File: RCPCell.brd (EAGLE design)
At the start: 99.8 x 80 mm, 22 parts, among them IC1 SIM900, Q1 BSS84, Q2 BSS84, U1 PESDXS4UD

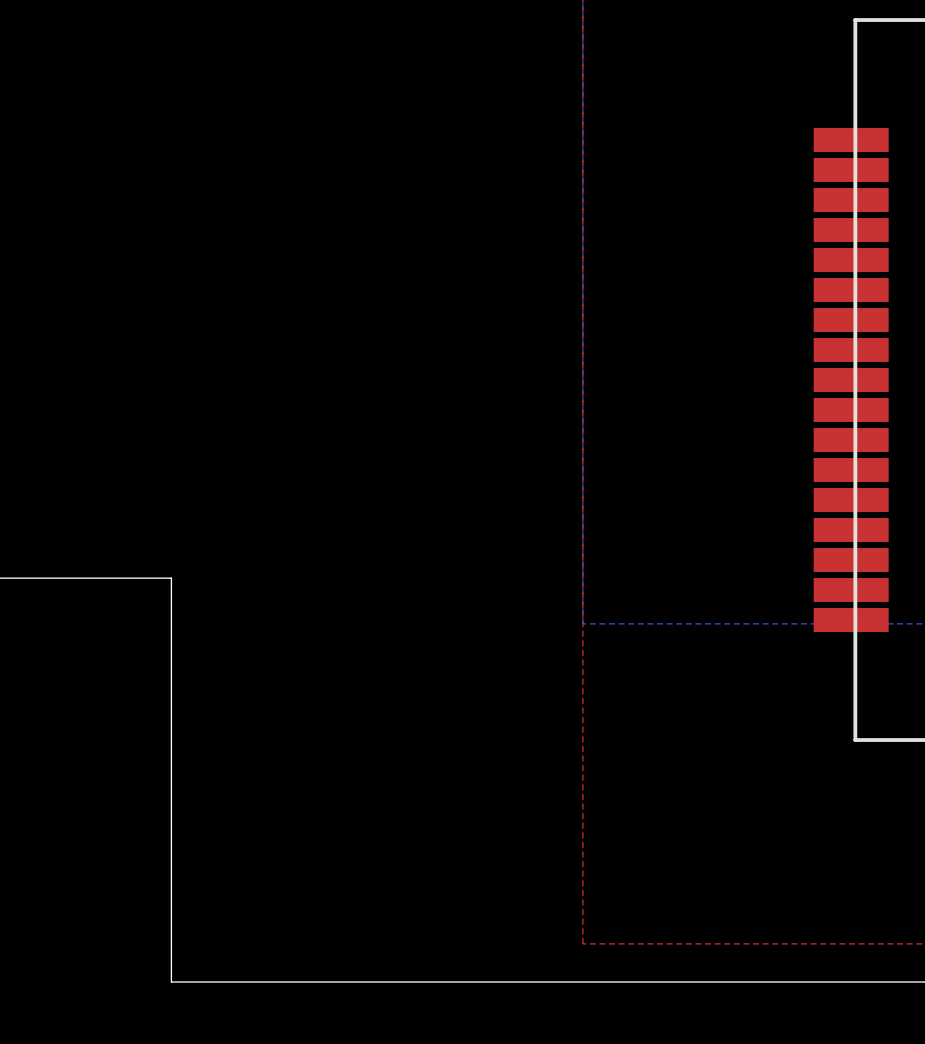
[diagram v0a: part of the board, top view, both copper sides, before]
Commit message: placeholder simcard
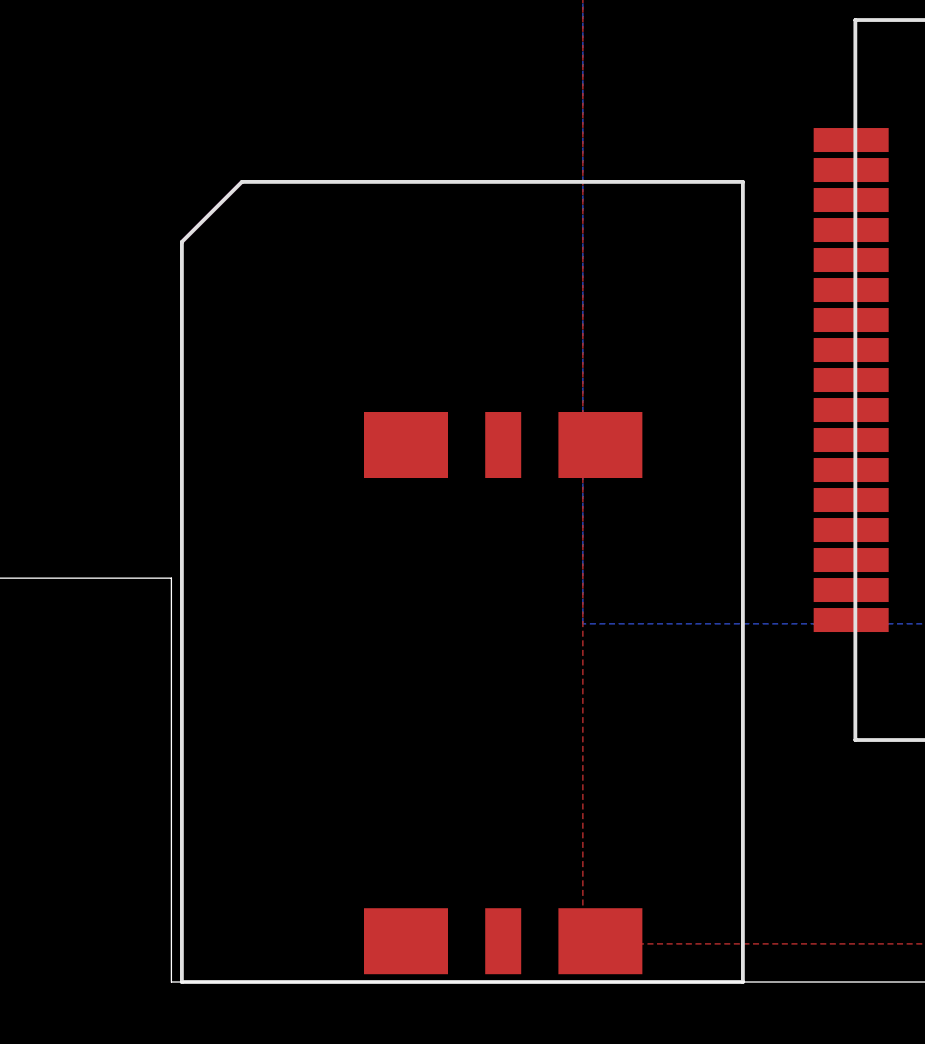
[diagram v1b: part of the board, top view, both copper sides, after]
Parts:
- added U$1: MOLEX_0470230001, simcard:MOLEX_0470230001
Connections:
- net GND: now also U$1.6
- net SIM_CLK_CARD: now also U$1.3
- net SIM_DATA_CARD: now also U$1.4
- net SIM_RST_CARD: now also U$1.2
- net SIM_VDD: now also U$1.1
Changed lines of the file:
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@@
 </element>
 <element name="J$1" library="SparkFun" package="SMA-EDGE" value="SMA_EDGE" x="74.168" y="3.8481"/>
+<element name="U$1" library="simcard" package="MOLEX_0470230001" value="MOLEX_0470230001" x="60.96" y="0" rot="R90"/>
 </elements>
 <signals>
@@
 <contactref element="J$1" pad="GND@1"/>
 <contactref element="J$1" pad="GND@0"/>
+<contactref element="U$1" pad="6"/>
 <wire x1="107.95" y1="72.136" x2="107.95" y2="74.676" width="0" layer="19" extent="1-1"/>
 <wire x1="100.418" y1="57.912" x2="107.95" y2="72.136" width="0" layer="19" extent="1-1"/>
@@
 <wire x1="93.726" y1="43.586" x2="88.392" y2="43.586" width="0" layer="19" extent="1-1"/>
 <wire x1="93.98" y1="43.586" x2="93.726" y2="43.586" width="0" layer="19" extent="1-1"/>
-<wire x1="84.708" y1="32.205" x2="88.392" y2="43.586" width="0" layer="19" extent="1-1"/>
-<wire x1="88.847" y1="28.066" x2="84.708" y2="32.205" width="0" layer="19" extent="1-1"/>
+<wire x1="93.98" y1="37.211" x2="93.726" y2="43.586" width="0" layer="19" extent="1-1"/>
+<wire x1="88.847" y1="28.066" x2="93.98" y2="37.211" width="0" layer="19" extent="1-1"/>
+<wire x1="84.708" y1="32.205" x2="88.847" y2="28.066" width="0" layer="19" extent="1-1"/>
 <wire x1="73.708" y1="32.205" x2="84.708" y2="32.205" width="0" layer="19" extent="1-1"/>
 <wire x1="70.104" y1="42.672" x2="73.708" y2="32.205" width="0" layer="19" extent="1-1"/>
 <wire x1="70.104" y1="46.158" x2="70.104" y2="47.244" width="0" layer="19" extent="1-1"/>
 <wire x1="67.056" y1="41.998" x2="70.104" y2="42.672" width="0" layer="19" extent="1-1"/>
-<wire x1="93.98" y1="37.211" x2="67.056" y2="41.998" width="0" layer="19" extent="1-1"/>
 <wire x1="64.569" y1="24.066" x2="73.708" y2="32.205" width="0" layer="19" extent="1-1"/>
 <wire x1="64.569" y1="18.066" x2="64.569" y2="24.066" width="0" layer="19" extent="1-1"/>
@@
 <wire x1="74.168" y1="3.8481" x2="74.168" y2="3.8481" width="0" layer="19" extent="1-16"/>
 <wire x1="82.804" y1="73.533" x2="86.766" y2="55.626" width="0" layer="19" extent="1-1"/>
-<wire x1="5.842" y1="16.51" x2="88.847" y2="28.066" width="0" layer="19" extent="1-1"/>
-<wire x1="5.842" y1="13.97" x2="5.842" y2="16.51" width="0" layer="19" extent="1-1"/>
+<wire x1="56.21" y1="17.9" x2="69.762" y2="5.842" width="0" layer="19" extent="1-1"/>
+<wire x1="5.842" y1="13.97" x2="56.21" y2="17.9" width="0" layer="19" extent="1-1"/>
+<wire x1="5.842" y1="16.51" x2="5.842" y2="13.97" width="0" layer="19" extent="1-1"/>
 </signal>
 <signal name="DIN">
@@
 <via x="68.326" y="34.29" extent="1-16" drill="0.4572"/>
 <via x="72.644" y="34.29" extent="1-16" drill="0.4572"/>
+<contactref element="U$1" pad="1"/>
 <wire x1="68.072" y1="34.544" x2="67.056" y2="40.298" width="0" layer="19" extent="1-1"/>
+<wire x1="56.21" y1="1.36" x2="68.072" y2="34.544" width="0" layer="19" extent="1-1"/>
 </signal>
 <signal name="SIM_DATA">
@@
 <wire x1="69.342" y1="45.466" x2="69.342" y2="45.97" width="0.254" layer="1"/>
 <wire x1="69.342" y1="45.97" x2="69.154" y2="46.158" width="0.254" layer="1"/>
+<contactref element="U$1" pad="4"/>
+<wire x1="49.73" y1="17.9" x2="72.0598" y2="37.934" width="0" layer="19" extent="1-1"/>
 </signal>
 <signal name="SIM_RST_CARD">
@@
 <wire x1="69.342" y1="37.934" x2="69.342" y2="43.57" width="0.254" layer="1"/>
 <wire x1="69.342" y1="43.57" x2="69.154" y2="43.758" width="0.254" layer="1"/>
+<contactref element="U$1" pad="2"/>
+<wire x1="52.97" y1="1.36" x2="69.342" y2="37.934" width="0" layer="19" extent="1-1"/>
 </signal>
 <signal name="SIM_CLK_CARD">
@@
 <wire x1="71.054" y1="43.758" x2="71.054" y2="44.262" width="0.254" layer="1"/>
 <wire x1="71.054" y1="44.262" x2="70.612" y2="44.704" width="0.254" layer="1"/>
+<contactref element="U$1" pad="3"/>
+<wire x1="49.73" y1="1.36" x2="70.7136" y2="41.2868" width="0" layer="19" extent="1-1"/>
 </signal>
 <signal name="N$3">

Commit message: WIP for MK2 version of cell module
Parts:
- U$1: value MOLEX_0470230001 -> MOLEX_04702300012; device simcard:MOLEX_0470230001 -> simcard:MOLEX_91228-3001
- moved C10 78.4 mm to (19.1, 23.6)
- moved C9 78.4 mm to (18.8, 23.6)
- moved C11 78.4 mm to (15.0, 32.5)
- moved C8 78.4 mm to (13.5, 23.6)
- moved NETLIGHT 71.8 mm to (71.1, 4.57), turned to 0 degrees
- moved R8 68.0 mm to (76.5, 2.54)
- moved Q1 31.3 mm to (90.4, 53.8), turned to 90 degrees
- moved R6 30.6 mm to (86.4, 53.8), turned to 180 degrees
- moved Q2 26.5 mm to (90.4, 58.7), turned to 90 degrees
- moved R7 26.4 mm to (86.4, 58.7), turned to 180 degrees
- moved EX1 8.98 mm to (87.8, 37.3), turned to 0 degrees
- moved U$1 8.52 mm to (53.3, 3.81), turned to 0 degrees
- moved C7 6.40 mm to (77.0, 5.08)
- moved C1 6.35 mm to (73.4, 41.1)
- moved IC1 6.35 mm to (83.1, 20.1)
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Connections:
- removed net N$2: NETLIGHT.A, R8.1
- new net N$1: NETLIGHT.C, R8.2
- net GND: now also R8.1; no longer NETLIGHT.C
- net STATUS: now also NETLIGHT.A; no longer R8.2
- net USB_DM_HS_OUT: now also EX1.3; no longer EX1.4
- net USB_DP_HS_OUT: now also EX1.4; no longer EX1.3
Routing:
- net N$2: track 3.68 -> 0.00 mm
- net V+: track 13.6 -> 11.2 mm
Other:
- outline, holes or cut-outs redrawn
- board text added: "Rev C"
- board text removed: "Rev B"

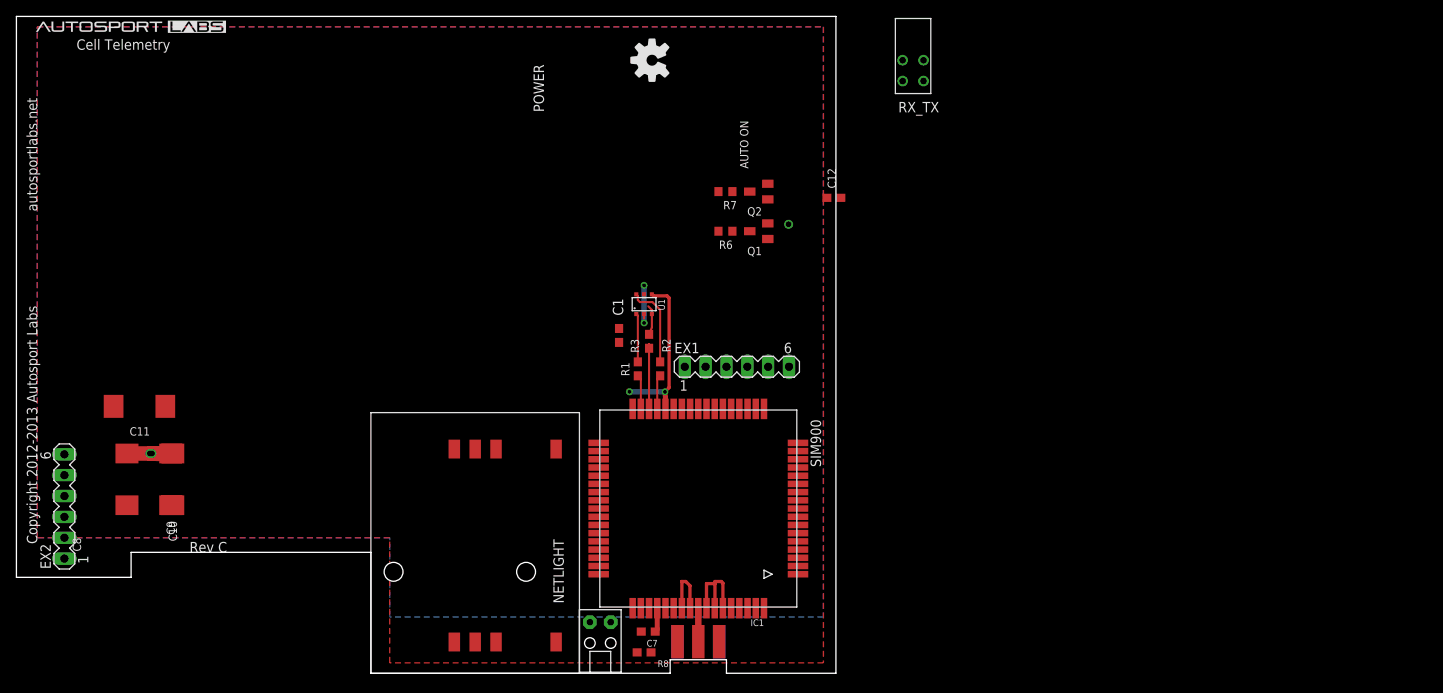
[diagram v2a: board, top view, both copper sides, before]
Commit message: WIP for cellular module, compacted board size
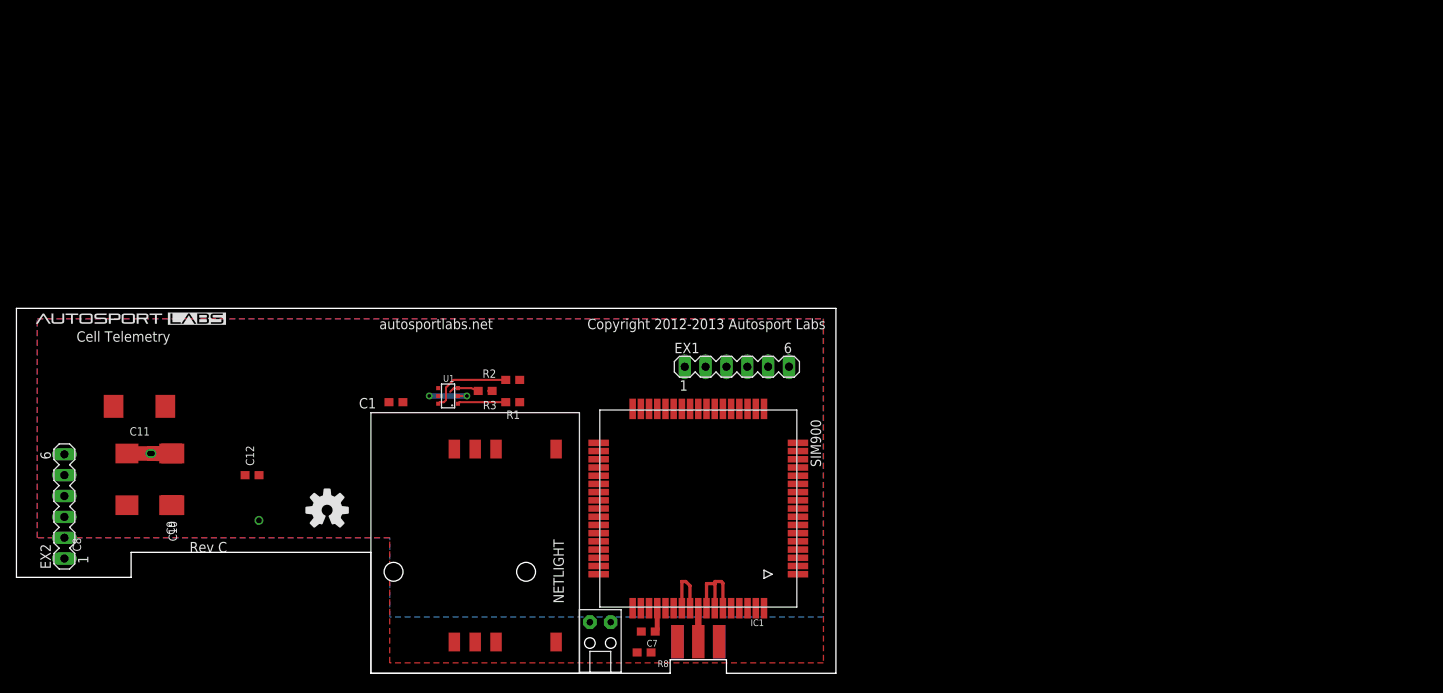
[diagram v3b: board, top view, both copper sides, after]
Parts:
- removed Q1, Q2: BSS84, transistor-small-signal:SOT23
- removed R6, R7: 180, rcl:R0603
- removed RX_TX: DUAL_PANEL_LED, LEDs:DUAL_PANEL_LED
- moved C12 78.5 mm to (28.7, 24.1)
- moved C1 28.4 mm to (46.2, 33.0), turned to 180 degrees
- moved U1 26.4 mm to (52.6, 33.8), turned to 90 degrees
- moved R3 20.9 mm to (57.1, 34.4), turned to 180 degrees
- moved R2 18.0 mm to (60.5, 35.7), turned to 0 degrees
- moved R1 15.8 mm to (60.5, 33.0), turned to 180 degrees
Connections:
- removed net N$3: Q2.3, R7.1
- removed net N$4: R6.2, RX_TX.1
- removed net N$5: Q1.3, R6.1
- removed net N$6: R7.2, RX_TX.3
- net DIN: no longer Q2.1
- net DOUT: no longer Q1.1
- net GND: no longer RX_TX.2, RX_TX.4
- net V+: no longer Q1.2, Q2.2
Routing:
- net SIM_VDD: track 20.7 -> 0.00 mm, vias 2 -> 0
- net SIM_CLK: track 8.39 -> 0.50 mm
- net SIM_DATA: track 4.17 -> 0.50 mm
- net SIM_RST: track 4.18 -> 0.52 mm
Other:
- board size 99.8 x 80 mm -> 99.8 x 44.5 mm
- board text removed: "AUTO ON"
- board text removed: "POWER"

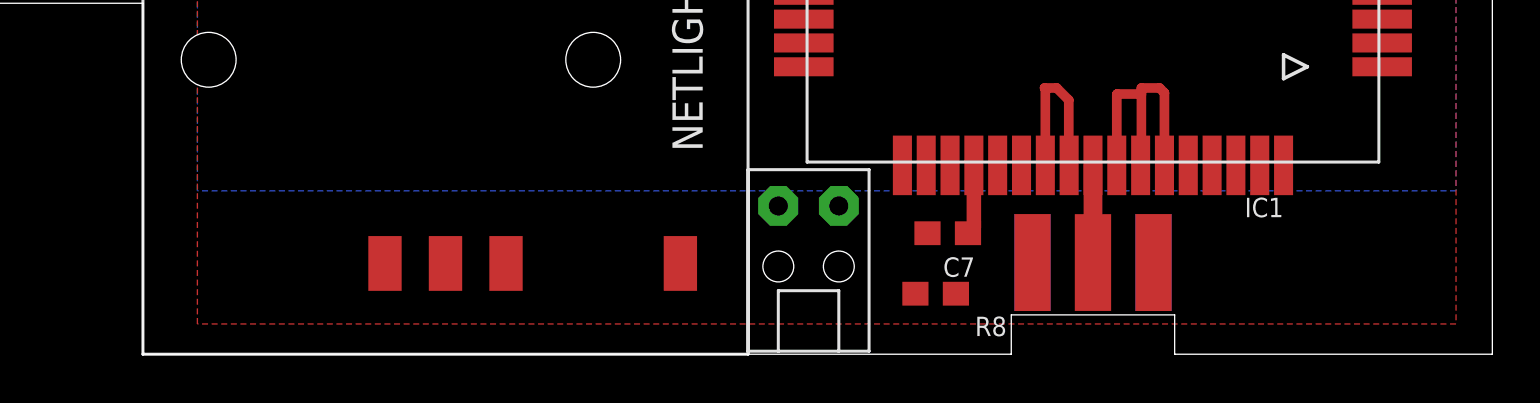
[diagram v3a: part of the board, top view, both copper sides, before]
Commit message: modified notch to account for bit radius
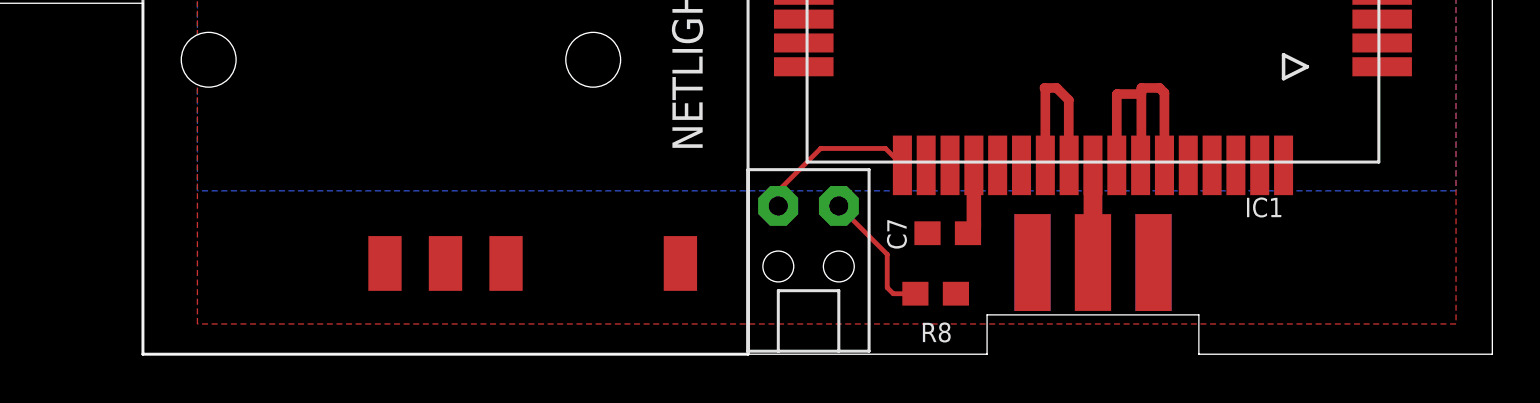
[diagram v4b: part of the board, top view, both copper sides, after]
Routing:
- net STATUS: track 0.00 -> 6.87 mm
- net N$1: track 0.00 -> 5.56 mm
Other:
- outline, holes or cut-outs redrawn
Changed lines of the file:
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@@
 <setting verticaltext="up"/>
 </settings>
-<grid distance="0.1" unitdist="inch" unit="inch" style="lines" multiple="1" display="no" altdistance="0.001" altunitdist="inch" altunit="inch"/>
+<grid distance="0.01" unitdist="inch" unit="inch" style="lines" multiple="1" display="no" altdistance="0.001" altunitdist="inch" altunit="inch"/>
 <layers>
 <layer number="1" name="Top" color="4" fill="1" visible="yes" active="yes"/>
@@
 <board>
 <plain>
-<wire x1="99.822" y1="0" x2="86.487" y2="0" width="0" layer="20"/>
-<wire x1="86.487" y1="0" x2="86.487" y2="1.651" width="0" layer="20"/>
-<wire x1="86.487" y1="1.651" x2="79.629" y2="1.651" width="0" layer="20"/>
-<wire x1="79.629" y1="1.651" x2="79.629" y2="0" width="0" layer="20"/>
-<wire x1="79.629" y1="0" x2="43.18" y2="0" width="0" layer="20"/>
+<wire x1="99.822" y1="0" x2="87.503" y2="0" width="0" layer="20"/>
+<wire x1="87.503" y1="0" x2="87.503" y2="1.651" width="0" layer="20"/>
+<wire x1="87.503" y1="1.651" x2="78.613" y2="1.651" width="0" layer="20"/>
+<wire x1="78.613" y1="1.651" x2="78.613" y2="0" width="0" layer="20"/>
+<wire x1="78.613" y1="0" x2="43.18" y2="0" width="0" layer="20"/>
 <wire x1="43.18" y1="0" x2="43.18" y2="14.732" width="0" layer="20"/>
 <wire x1="43.18" y1="14.732" x2="13.97" y2="14.732" width="0" layer="20"/>
@@
 <elements>
 <element name="R8" library="SparkFun" package="0603" value="180" x="76.454" y="2.54" smashed="yes" rot="R180">
-<attribute name="NAME" x="78.105" y="0.762" size="0.8128" layer="25" font="vector"/>
+<attribute name="NAME" x="75.819" y="0.508" size="0.8128" layer="25" font="vector"/>
 </element>
 <element name="NETLIGHT" library="LEDs" package="RIGHTANGLE_CML_5323F5" value="PANEL_LED" x="71.12" y="4.572" smashed="yes">
@@
 </element>
 <element name="C7" library="rcl" package="C0603" value="0.1uf" x="76.962" y="5.08" smashed="yes" rot="R180">
-<attribute name="NAME" x="78.105" y="4.064" size="0.8128" layer="25" rot="R180"/>
+<attribute name="NAME" x="74.422" y="5.715" size="0.8128" layer="25" rot="R270"/>
 </element>
 <element name="R2" library="SparkFun" package="0603" value="27" x="60.452" y="35.7378" smashed="yes">
@@
 <contactref element="IC1" pad="52"/>
 <contactref element="NETLIGHT" pad="A"/>
-<wire x1="69.85" y1="6.223" x2="75.058" y2="7.927" width="0" layer="19" extent="1-1"/>
+<wire x1="75.058" y1="7.927" x2="74.349" y2="8.636" width="0.2032" layer="1"/>
+<wire x1="74.349" y1="8.636" x2="71.628" y2="8.636" width="0.2032" layer="1"/>
+<wire x1="71.628" y1="8.636" x2="69.85" y2="6.858" width="0.2032" layer="1"/>
+<wire x1="69.85" y1="6.858" x2="69.85" y2="6.223" width="0.2032" layer="1"/>
 </signal>
 <signal name="SIM_VDD">
@@
 <contactref element="R8" pad="2"/>
 <contactref element="NETLIGHT" pad="C"/>
-<wire x1="72.39" y1="6.223" x2="75.604" y2="2.54" width="0" layer="19" extent="1-1"/>
+<wire x1="72.39" y1="6.223" x2="74.422" y2="4.191" width="0.2032" layer="1"/>
+<wire x1="74.422" y1="4.191" x2="74.422" y2="2.794" width="0.2032" layer="1"/>
+<wire x1="74.422" y1="2.794" x2="74.676" y2="2.54" width="0.2032" layer="1"/>
+<wire x1="74.676" y1="2.54" x2="75.604" y2="2.54" width="0.2032" layer="1"/>
 </signal>
 </signals>

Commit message: final layout before incorporating power supply section
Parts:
- moved C1 33.2 mm to (69.6, 9.40), turned to 90 degrees
- moved C8 27.3 mm to (37.8, 35.8), turned to 90 degrees
- moved C12 19.1 mm to (9.78, 21.5), turned to 270 degrees
- moved C9 18.4 mm to (32.6, 35.8), turned to 90 degrees
- moved C10 14.9 mm to (27.6, 35.8), turned to 90 degrees
- moved C11 11.2 mm to (13.3, 21.5), turned to 270 degrees
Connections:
- net +5V: no longer C11.+
- net SAFE12V: now also C11.+, C12.1
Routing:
- net SIM_VDD: track 0.00 -> 92.2 mm, vias 0 -> 5
- net SIM_CLK_CARD: track 3.67 -> 34.4 mm, vias 0 -> 2
- net SIM_RST_CARD: track 5.90 -> 35.5 mm, vias 0 -> 2
- net SIM_CLK: track 0.50 -> 25.0 mm, vias 0 -> 2
- net SIM_DATA: track 0.50 -> 19.2 mm, vias 0 -> 2
- net SIM_RST: track 0.52 -> 19.0 mm, vias 0 -> 2
- net SAFE12V: track 0.00 -> 12.6 mm
- net V+: track 11.2 -> 20.6 mm
- net SIM_DATA_CARD: track 10.3 -> 16.7 mm
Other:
- board text added: "Copyright 2012-2014 Autosport Labs"
- board text removed: "Copyright 2012-2013 Autosport Labs"
